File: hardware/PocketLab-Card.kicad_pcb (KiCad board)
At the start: 4 copper layers, 85.6 x 54 mm, 267 parts, among them J1 USB-C DATA/POWER, J2 microSD, J3 EXTERNAL 400uH LF COIL, J4 PROTECTED 1S LiPo 3.7V, J5 30-PIN 2.54mm DUPONT GRID, J8 ER-OLED0.42-1W 72x40 SSD1306B, Q1 AO3400A IR DRIVER, Q2 CSD16406Q3 DISCHARGE, Q3 CSD16406Q3 CHARGE, SW1 RESET, SW2 BOOT, SW3 UP, SW4 DOWN, SW5 MAIN POWER OFF / ON, SW6 PAIR, SW7 SELECT, U1 ESP32-S3-WROOM-1-N8R2, U10 BMI270 (FULL OPTION), U11 BMP390 (FULL OPTION), U12 PCF8563T, U13 TSOP75338WTR 38kHz, U14 BQ29700DSE, U15 TPS2553DBVR 500mA LIMIT, U16 USBLC6-4SC6Y, U17 TPS22919DCKR LF 5V LOAD SWITCH, U18 TCA9534PWR INTERNAL CONTROL, U19 SRV05-4MR6T1G SD ESD, U2 PN5321A3HN/C106, U20 SN74AHCT1G126DBVR RGB LEVEL S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, U21 SN74LV125ATPWR LF/SPI 3V3-TO-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, U22 SN74LVC1G126DBVR LF 5V-TO-3V3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, U23 ATECC608C-SSHDA-T, U24 SRV05-4MR6T1G J5 BUS ESD, U25 SRV05-4MR6T1G J5 SPI ESD, U3 E07-900MM10S 855-925MHz, U4 HTRC11001T/03EE,11 125kHz, U5 BQ24074RGTR, U6 TPS63070RNMR 3V3, U7 TPS61023DRLR 5V BOOST, U8 MAX17048G+T10, U9 TCA9535PWR, Y301 27.12MHz crystal (pins 2/4 sh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, Y501 4MHz 5V CMOS OSCILLATOR, Y701 32.768kHz CL=7pF

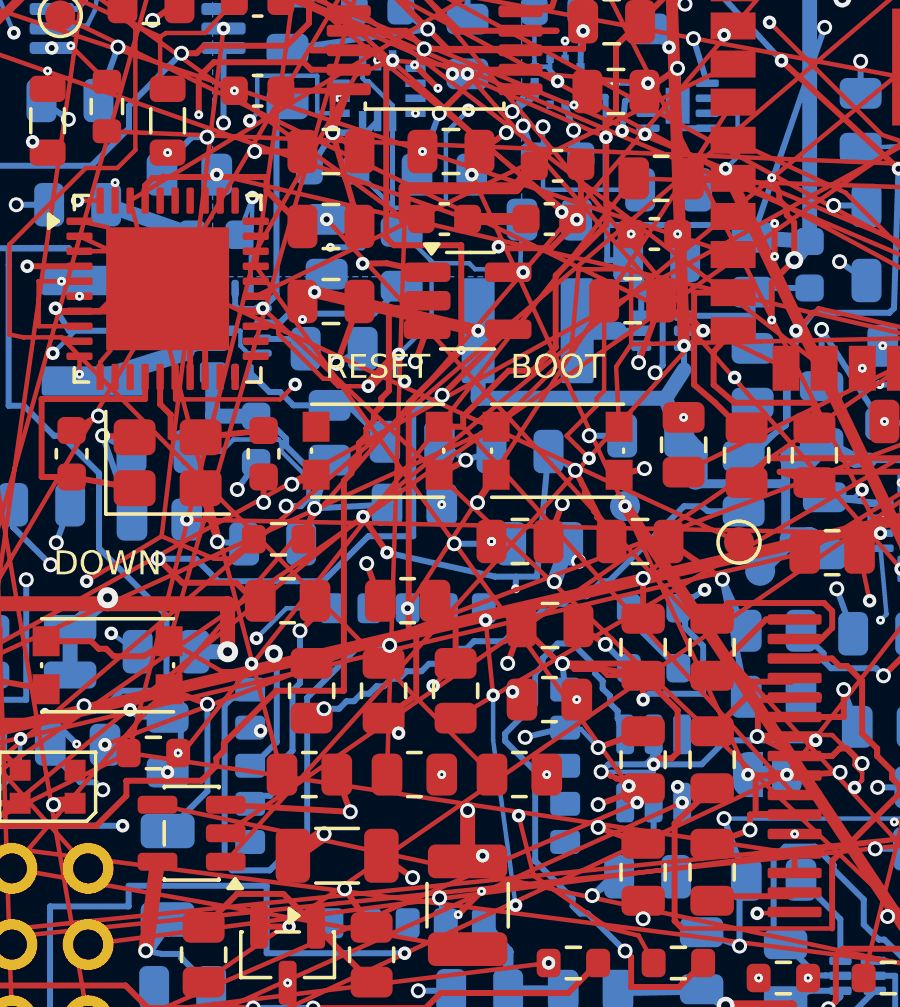
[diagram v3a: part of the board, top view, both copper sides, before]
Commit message: Relocate clustered OLED routing vias
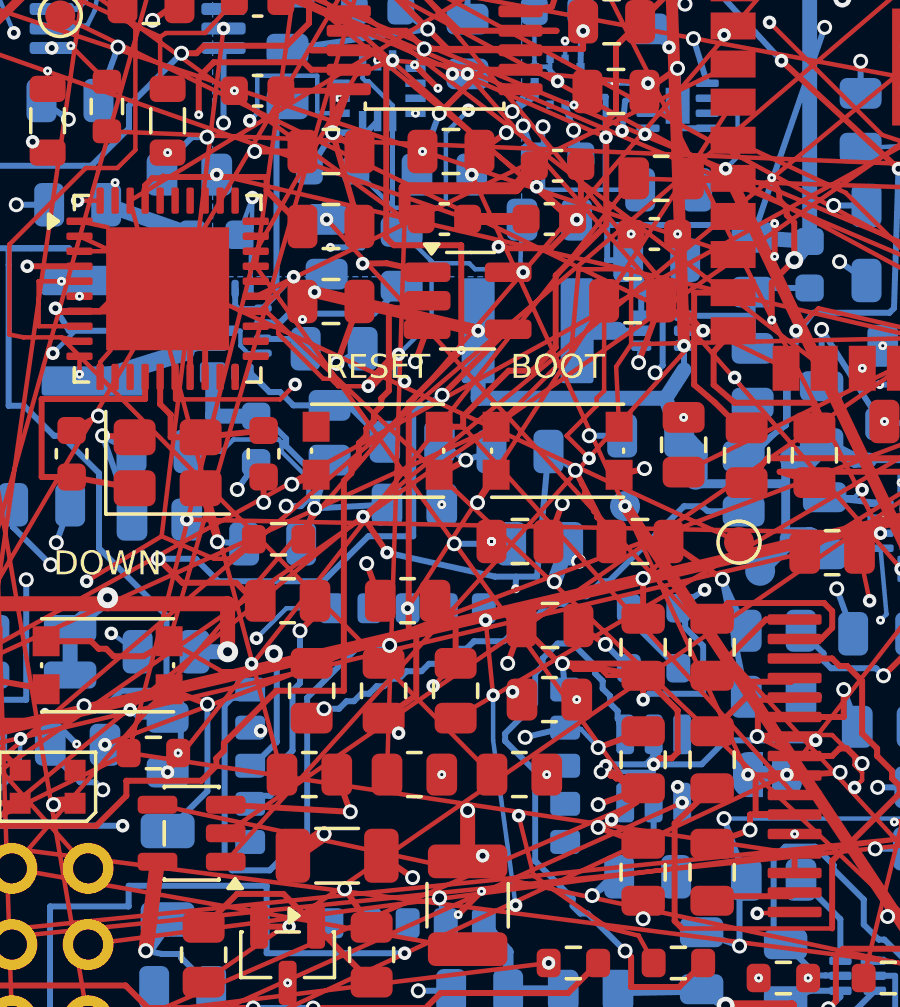
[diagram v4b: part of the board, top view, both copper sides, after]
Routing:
- net /U6_PS_SYNC: track 43.8 -> 46.7 mm
- net /CHARGER_CHG_N: track 47.2 -> 49.5 mm
- net /I2C_SCL: track 124.1 -> 126.2 mm
- net /SPI_MOSI_HDR: track 39.5 -> 41.5 mm
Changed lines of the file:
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@@
 	)
 	(via
-		(at 68.175 43.25)
+		(at 69.2 42.2)
 		(size 0.45)
 		(drill 0.2)
@@
 	)
 	(via
-		(at 80.375 59.175)
+		(at 79.6 58.5)
 		(size 0.45)
 		(drill 0.2)
@@
 	)
 	(via
-		(at 78.1375 40.045)
+		(at 77.3 39.2)
 		(size 0.45)
 		(drill 0.2)
@@
 	)
 	(via
-		(at 80.65 59.7275)
+		(at 79.8 60.3)
 		(size 0.45)
 		(drill 0.2)
@@
 		(net "/BOOST5_EN")
 	)
+	(segment
+		(start 80.65 59.7275)
+		(end 79.8 60.3)
+		(width 0.15)
+		(locked yes)
+		(layer "F.Cu")
+		(net "/SPI_MOSI_HDR")
+	)
+	(segment
+		(start 80.65 59.7275)
+		(end 79.8 60.3)
+		(width 0.15)
+		(locked yes)
+		(layer "In1.Cu")
+		(net "/SPI_MOSI_HDR")
+	)
+	(segment
+		(start 80.375 59.175)
+		(end 79.6 58.5)
+		(width 0.15)
+		(locked yes)
+		(layer "F.Cu")
+		(net "/I2C_SCL")
+	)
+	(segment
+		(start 80.375 59.175)
+		(end 79.6 58.5)
+		(width 0.15)
+		(locked yes)
+		(layer "In1.Cu")
+		(net "/I2C_SCL")
+	)
+	(segment
+		(start 78.1375 40.045)
+		(end 77.3 39.2)
+		(width 0.15)
+		(locked yes)
+		(layer "F.Cu")
+		(net "/CHARGER_CHG_N")
+	)
+	(segment
+		(start 78.1375 40.045)
+		(end 77.3 39.2)
+		(width 0.15)
+		(locked yes)
+		(layer "In2.Cu")
+		(net "/CHARGER_CHG_N")
+	)
+	(segment
+		(start 68.175 43.25)
+		(end 69.2 42.2)
+		(width 0.15)
+		(locked yes)
+		(layer "F.Cu")
+		(net "/U6_PS_SYNC")
+	)
+	(segment
+		(start 68.175 43.25)
+		(end 69.2 42.2)
+		(width 0.15)
+		(locked yes)
+		(layer "B.Cu")
+		(net "/U6_PS_SYNC")
+	)
 	(zone

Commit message: Move OLED I2C routing away from drill conflicts
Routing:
- net /I2C_SCL: track 126.2 -> 128.2 mm
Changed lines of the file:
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@@
 	)
 	(via
-		(at 79.6 58.5)
+		(at 80.8 61.2)
 		(size 0.45)
 		(drill 0.2)
@@
 	(segment
 		(start 80.375 59.175)
-		(end 79.6 58.5)
+		(end 80.8 61.2)
 		(width 0.15)
 		(locked yes)
@@
 	(segment
 		(start 80.375 59.175)
-		(end 79.6 58.5)
-		(width 0.15)
-		(locked yes)
+		(end 80.8 61.2)
+		(width 0.15)
+		(locked yes)
